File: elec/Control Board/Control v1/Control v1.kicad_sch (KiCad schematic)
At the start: 69 parts, among them J1 DB9_Female_MountingHoles, J10 Conn_02x12_Odd_Even, J11 Screw_Terminal_01x02, J14 Conn_01x10, J2 Conn_01x08, J25 Screw_Terminal_01x02, J3 Conn_01x08, J4 Conn_01x08, J5 Conn_01x08, J6 Conn_01x08, J7 Conn_01x10, J8 Conn_02x18_Odd_Even, J9 Conn_01x10

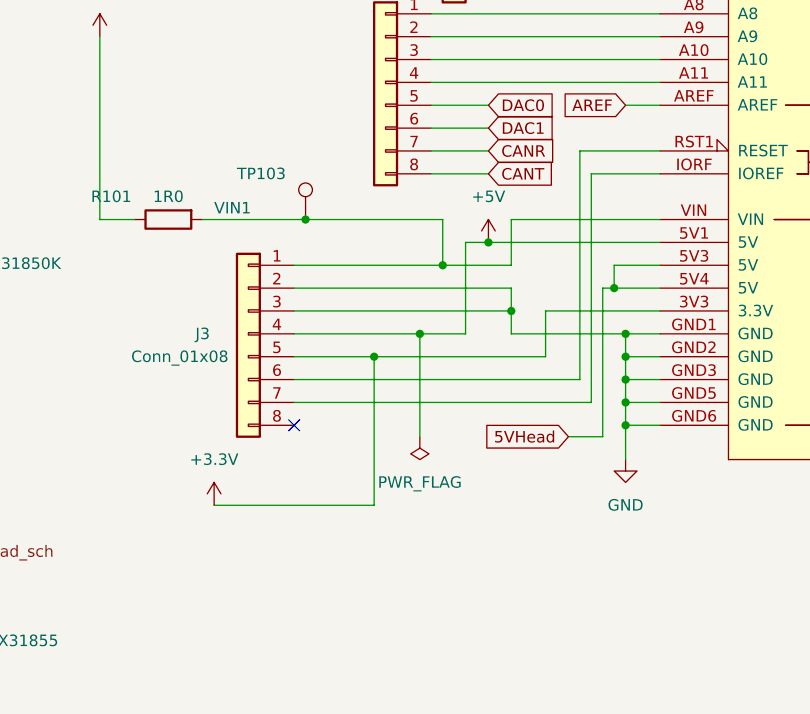
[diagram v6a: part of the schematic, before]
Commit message: Fixing some DRC errors on PCB.
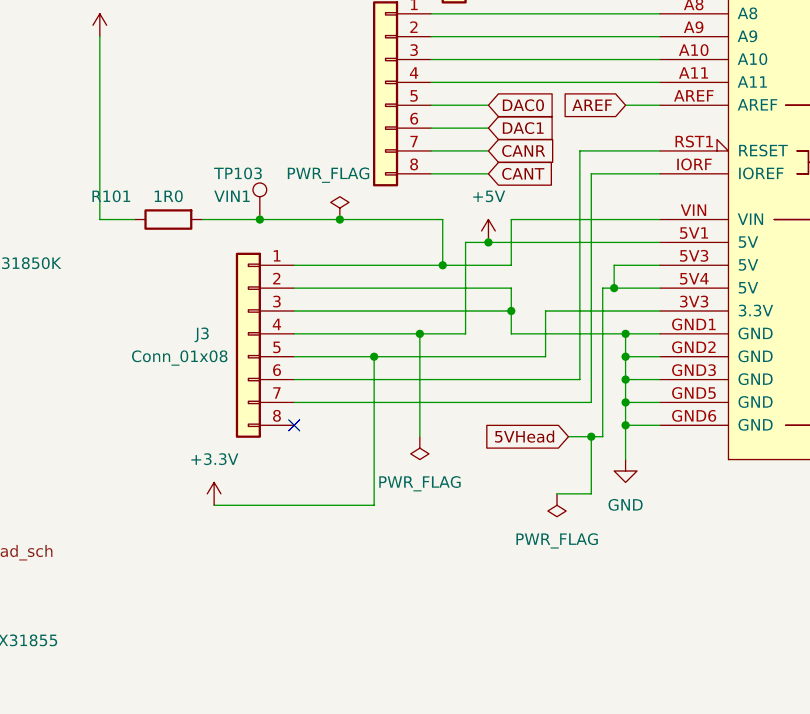
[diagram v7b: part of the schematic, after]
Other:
- moved on the sheet: TP103
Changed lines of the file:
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@@
     (comment 1 "Contributor: Lawrence Kinceloe")
   )
+  (junction (at 170.18 172.72) (diameter 0) (color 0 0 0 0)
+  )
   (junction (at 350.52 86.36) (diameter 0) (color 0 0 0 0)
   )
@@
   (junction (at 207.01 209.55) (diameter 0) (color 0 0 0 0)
   )
+  (junction (at 133.35 148.59) (diameter 0) (color 0 0 0 0)
+  )
   (junction (at 173.99 166.37) (diameter 0) (color 0 0 0 0)
   )
@@
   (junction (at 63.5 63.5) (diameter 0) (color 0 0 0 0)
   )
+  (junction (at 142.24 148.59) (diameter 0) (color 0 0 0 0)
+  )
   (junction (at 350.52 83.82) (diameter 0) (color 0 0 0 0)
   )
@@
   (junction (at 207.01 217.17) (diameter 0) (color 0 0 0 0)
   )
-  (junction (at 138.43 148.59) (diameter 0) (color 0 0 0 0)
-  )
   (junction (at 135.89 62.23) (diameter 0) (color 0 0 0 0)
   )
@@
     (stroke (width 0) (type default))
   )
+  (wire (pts (xy 142.24 148.59) (xy 153.67 148.59))
+    (stroke (width 0) (type default))
+  )
   (wire (pts (xy 243.84 125.73) (xy 246.38 125.73))
     (stroke (width 0) (type default))
@@
     (stroke (width 0) (type default))
   )
+  (wire (pts (xy 166.37 179.07) (xy 170.18 179.07))
+    (stroke (width 0) (type default))
+  )
   (wire (pts (xy 133.35 223.52) (xy 125.73 223.52))
     (stroke (width 0) (type default))
@@
     (stroke (width 0) (type default))
   )
-  (wire (pts (xy 167.64 172.72) (xy 171.45 172.72))
+  (wire (pts (xy 167.64 172.72) (xy 170.18 172.72))
+    (stroke (width 0) (type default))
+  )
+  (wire (pts (xy 170.18 179.07) (xy 170.18 172.72))
     (stroke (width 0) (type default))
   )
@@
     (stroke (width 0) (type default))
   )
-  (wire (pts (xy 127 148.59) (xy 138.43 148.59))
+  (wire (pts (xy 127 148.59) (xy 133.35 148.59))
     (stroke (width 0) (type default))
   )
@@
     (stroke (width 0) (type default))
   )
-  (wire (pts (xy 138.43 148.59) (xy 153.67 148.59))
+  (wire (pts (xy 133.35 148.59) (xy 142.24 148.59))
     (stroke (width 0) (type default))
   )
@@
     (stroke (width 0) (type default))
   )
+  (wire (pts (xy 170.18 172.72) (xy 171.45 172.72))
+    (stroke (width 0) (type default))
+  )
   (wire (pts (xy 381 45.72) (xy 381 66.04))
     (stroke (width 0) (type default))
@@
     )
   )
+  (symbol (lib_id "power:PWR_FLAG") (at 142.24 148.59 0) (unit 1)
+    (in_bom yes) (on_board yes) (dnp no)
+    (property "Reference" "#FLG07" (at 142.24 146.685 0)
+      (effects (font (size 1.27 1.27)) hide)
+    )
+    (property "Value" "PWR_FLAG" (at 140.97 143.51 0)
+      (effects (font (size 1.27 1.27)))
+    )
+    (property "Footprint" "" (at 142.24 148.59 0)
+      (effects (font (size 1.27 1.27)) hide)
+    )
+    (property "Datasheet" "~" (at 142.24 148.59 0)
+      (effects (font (size 1.27 1.27)) hide)
+    )
+    (pin "1")
+    (instances
+      (project "Control v1"
+        (path "/c68c9deb-8d4d-42f0-adf8-4d3022f4ee59"
+          (reference "#FLG07") (unit 1)
+        )
+      )
+    )
+  )
   (symbol (lib_id "power:GND") (at 173.99 175.26 0) (unit 1)
     (in_bom yes) (on_board yes) (dnp no) (fields_autoplaced)
@@
     )
   )
-  (symbol (lib_id "Connector:TestPoint") (at 138.43 148.59 0) (unit 1)
+  (symbol (lib_id "Connector:TestPoint") (at 133.35 148.59 0) (unit 1)
     (in_bom yes) (on_board yes) (dnp no)
-    (property "Reference" "TP103" (at 130.81 143.51 0)
+    (property "Reference" "TP103" (at 128.27 143.51 0)
       (effects (font (size 1.27 1.27)) (justify left))
     )
-    (property "Value" "VIN1" (at 128.27 147.32 0)
+    (property "Value" "VIN1" (at 128.27 146.05 0)
       (effects (font (size 1.27 1.27)) (justify left))
     )
-    (property "Footprint" "TestPoint:TestPoint_Loop_D2.54mm_Drill1.5mm_Beaded" (at 143.51 148.59 0)
+    (property "Footprint" "TestPoint:TestPoint_Loop_D2.54mm_Drill1.5mm_Beaded" (at 138.43 148.59 0)
       (effects (font (size 1.27 1.27)) hide)
     )
-    (property "Datasheet" "~" (at 143.51 148.59 0)
+    (property "Datasheet" "~" (at 138.43 148.59 0)
       (effects (font (size 1.27 1.27)) hide)
     )
-    (property "AssemblyType" "HAND" (at 138.43 148.59 0)
+    (property "AssemblyType" "HAND" (at 133.35 148.59 0)
       (effects (font (size 1.27 1.27)) hide)
     )
@@
         )
       )
+    )
+  )
+  (symbol (lib_id "power:PWR_FLAG") (at 166.37 179.07 180) (unit 1)
+    (in_bom yes) (on_board yes) (dnp no) (fields_autoplaced)
+    (property "Reference" "#FLG02" (at 166.37 180.975 0)
+      (effects (font (size 1.27 1.27)) hide)
+    )
+    (property "Value" "PWR_FLAG" (at 166.37 184.15 0)
+      (effects (font (size 1.27 1.27)))
+    )
+    (property "Footprint" "" (at 166.37 179.07 0)
+      (effects (font (size 1.27 1.27)) hide)
+    )
+    (property "Datasheet" "~" (at 166.37 179.07 0)
+      (effects (font (size 1.27 1.27)) hide)
+    )
+    (pin "1")
+    (instances
+      (project "Control v1"
+        (path "/c68c9deb-8d4d-42f0-adf8-4d3022f4ee59"
+          (reference "#FLG02") (unit 1)
+        )
+      )

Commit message: Update parts in schematic for BOM generation.
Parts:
- J1: AssemblyType (none) -> HAND; Cost (none) -> 0.2718; Distributor 1 (none) -> JLCPCB; Distributor 1 PN (none) -> C141882; MPN (none) -> D-DMR009PF-D002; Manufacturer (none) -> Ckmtw(Shenzhen Cankemeng)
- J10: Cost (none) -> 1000000; Distributor 2 JLCPCB -> JLCPCB ?https://jlcpcb.com/partdetail/566831-B24B_XADSS_N_A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; Distributor 2 PN https://jlcpcb.com/partdetail/Cnjm-CNJMA2006WV_2X12P9T/C283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 -> ? https://jlcpcb.com/partdetail/Cnjm-CNJMA2006WV_2X12P9T/C2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
- J11, J25: Distributor 1 PN C2915639 -> C918120; MPN (none) -> DB125-2.54-2P-GN-S; Manufacturer (none) -> DIBO
- J8: AssemblyType (none) -> HAND; Cost (none) -> 0.3441; Distributor 1 (none) -> JLCPCB; Distributor 1 PN (none) -> C132131
- R101: Cost 0.0015 -> 0.0012; Distributor 1 PN (none) -> C23163; MPN RMC060315%N -> 0603WAF4704T5E
- TP103: Cost (none) -> NA
- TP103: Cost (none) -> 0
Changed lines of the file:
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@@
       (effects (font (size 1.27 1.27)) hide)
     )
-    (property "Datasheet" "~" (at 312.42 138.43 0)
+    (property "Datasheet" "C132131_DS1023-2_18SF11.pdf" (at 312.42 138.43 0)
+      (effects (font (size 1.27 1.27)) hide)
+    )
+    (property "AssemblyType" "HAND" (at 312.42 138.43 0)
+      (effects (font (size 1.27 1.27)) hide)
+    )
+    (property "Cost" "0.3441" (at 312.42 138.43 0)
+      (effects (font (size 1.27 1.27)) hide)
+    )
+    (property "Description" "2.54mm 2.54mm 双排 36P Straight 2x18P Plugin,P=2.54mm Female Headers ROHS" (at 312.42 138.43 0)
+      (effects (font (size 1.27 1.27)) hide)
+    )
+    (property "Distributor 1" "JLCPCB" (at 312.42 138.43 0)
+      (effects (font (size 1.27 1.27)) hide)
+    )
+    (property "Distributor 1 PN" "C132131" (at 312.42 138.43 0)
       (effects (font (size 1.27 1.27)) hide)
     )
@@
       (effects (font (size 1.27 1.27)) hide)
     )
+    (property "Cost" "NA" (at 193.04 39.37 0)
+      (effects (font (size 1.27 1.27)) hide)
+    )
     (pin "1")
     (instances
@@
       (effects (font (size 1.27 1.27)) hide)
     )
+    (property "Cost" "NA" (at 135.89 57.15 0)
+      (effects (font (size 1.27 1.27)) hide)
+    )
     (pin "1")
     (instances
@@
       (effects (font (size 1.27 1.27)) hide)
     )
+    (property "Cost" "NA" (at 48.26 41.91 0)
+      (effects (font (size 1.27 1.27)) hide)
+    )
     (pin "1")
     (instances
@@
       (effects (font (size 1.27 1.27)) hide)
     )
-    (property "Distributor 1 PN" "C2915639" (at 394.97 205.74 0)
+    (property "Distributor 1 PN" "C918120" (at 394.97 205.74 0)
+      (effects (font (size 1.27 1.27)) hide)
+    )
+    (property "MPN" "DB125-2.54-2P-GN-S" (at 394.97 205.74 0)
+      (effects (font (size 1.27 1.27)) hide)
+    )
+    (property "Manufacturer" "DIBO" (at 394.97 205.74 0)
       (effects (font (size 1.27 1.27)) hide)
     )
@@
       (effects (font (size 1.27 1.27)) hide)
     )
+    (property "Cost" "NA" (at 129.54 48.26 0)
+      (effects (font (size 1.27 1.27)) hide)
+    )
     (pin "1")
     (instances
@@
       (effects (font (size 1.27 1.27)) hide)
     )
+    (property "Cost" "NA" (at 133.35 148.59 0)
+      (effects (font (size 1.27 1.27)) hide)
+    )
     (pin "1")
     (instances
@@
       (effects (font (size 1.27 1.27)) hide)
     )
-    (property "Datasheet" "~" (at 190.5 218.44 0)
+    (property "Datasheet" "C23163_0603WAF4704T5E.pdf" (at 190.5 218.44 0)
       (effects (font (size 1.27 1.27)) hide)
     )
@@
       (effects (font (size 1.27 1.27)) hide)
     )
-    (property "Distributor 1 PN" "" (at 190.5 218.44 90)
+    (property "Distributor 1 PN" "C23163" (at 190.5 218.44 90)
       (effects (font (size 1.27 1.27)) hide)
     )
@@
       (effects (font (size 1.27 1.27)) hide)
     )
-    (property "MPN" "RMC060315%N" (at 190.5 218.44 90)
+    (property "MPN" "0603WAF4704T5E" (at 190.5 218.44 90)
       (effects (font (size 1.27 1.27)) hide)
     )
-    (property "Description" "0.1W ±5% 1Ω 0603 Chip Resistor - Surface Mount ROHS" (at 190.5 218.44 0)
+    (property "Description" "100mW Thick Film Resistors ±100ppm/℃ ±1% 4.7MΩ 0603 Chip Resistor - Surface Mount ROHS" (at 190.5 218.44 0)
       (effects (font (size 1.27 1.27)) hide)
     )
@@
       (effects (font (size 1.27 1.27)) hide)
     )
-    (property "Cost" "0.0015" (at 190.5 218.44 0)
+    (property "Cost" "0.0012" (at 190.5 218.44 0)
       (effects (font (size 1.27 1.27)) hide)
     )
@@
       (effects (font (size 1.27 1.27)) hide)
     )
+    (property "Cost" "0" (at 154.94 59.69 0)
+      (effects (font (size 1.27 1.27)) hide)
+    )
     (pin "1")
     (instances
@@
       (effects (font (size 1.27 1.27)) hide)
     )
-    (property "Distributor 1 PN" "C2915639" (at 394.97 173.99 0)
+    (property "Distributor 1 PN" "C918120" (at 394.97 173.99 0)
+      (effects (font (size 1.27 1.27)) hide)
+    )
+    (property "MPN" "DB125-2.54-2P-GN-S" (at 394.97 173.99 0)
+      (effects (font (size 1.27 1.27)) hide)
+    )
+    (property "Manufacturer" "DIBO" (at 394.97 173.99 0)
       (effects (font (size 1.27 1.27)) hide)
     )
@@
       (effects (font (size 1.27 1.27)) hide)
     )
-    (property "Distributor 2" "JLCPCB" (at 368.3 78.74 0)
+    (property "Distributor 2" "JLCPCB ?https://jlcpcb.com/partdetail/566831-B24B_XADSS_N_A_LF_SN/C545730?" (at 368.3 78.74 0)
+      (effects (font (size 1.27 1.27)) hide)
+    )
+    (property "Distributor 2 PN" "?  https://jlcpcb.com/partdetail/Cnjm-CNJMA2006WV_2X12P9T/C2834570 ?" (at 368.3 78.74 0)
       (effects (font (size 1.27 1.27)) hide)
     )
-    (property "Distributor 2 PN" "https://jlcpcb.com/partdetail/Cnjm-CNJMA2006WV_2X12P9T/C2834570" (at 368.3 78.74 0)
+    (property "Cost" "1000000" (at 368.3 78.74 0)
       (effects (font (size 1.27 1.27)) hide)
     )
@@
       (effects (font (size 1.27 1.27)) hide)
     )
+    (property "Cost" "0" (at 162.56 59.69 0)
+      (effects (font (size 1.27 1.27)) hide)
+    )
     (pin "1")
     (instances
@@
       (effects (font (size 1.27 1.27)) hide)
     )
-    (property "Distributor 1 PN" "C2915639" (at 394.97 234.95 0)
+    (property "Distributor 1 PN" "C918120" (at 394.97 234.95 0)
+      (effects (font (size 1.27 1.27)) hide)
+    )
+    (property "MPN" "DB125-2.54-2P-GN-S" (at 394.97 234.95 0)
+      (effects (font (size 1.27 1.27)) hide)
+    )
+    (property "Manufacturer" "DIBO" (at 394.97 234.95 0)
       (effects (font (size 1.27 1.27)) hide)
     )
@@
       (effects (font (size 1.27 1.27)) hide)
     )
-    (property "Datasheet" " ~" (at 46.99 71.12 0)
+    (property "Datasheet" "C141882_D-DMR009PF-D002.pdf" (at 46.99 71.12 0)
+      (effects (font (size 1.27 1.27)) hide)
+    )
+    (property "AssemblyType" "HAND" (at 46.99 71.12 0)
+      (effects (font (size 1.27 1.27)) hide)
+    )
+    (property "Cost" "0.2718" (at 46.99 71.12 0)
+      (effects (font (size 1.27 1.27)) hide)
+    )
+    (property "Description" "9P Female D-Sub Shrouded 2 3A -50℃~+105℃ Plugin D-Sub/DVI/HDMI Connectors ROHS" (at 46.99 71.12 0)
+      (effects (font (size 1.27 1.27)) hide)
+    )
+    (property "Distributor 1" "JLCPCB" (at 46.99 71.12 0)
+      (effects (font (size 1.27 1.27)) hide)
+    )
+    (property "Distributor 1 PN" "C141882" (at 46.99 71.12 0)
+      (effects (font (size 1.27 1.27)) hide)
+    )
+    (property "MPN" "D-DMR009PF-D002" (at 46.99 71.12 0)
+      (effects (font (size 1.27 1.27)) hide)
+    )
+    (property "Manufacturer" "Ckmtw(Shenzhen Cankemeng)" (at 46.99 71.12 0)
       (effects (font (size 1.27 1.27)) hide)
     )
@@
       (effects (font (size 1.27 1.27)) hide)
     )
-    (property "Distributor 1 PN" "C2915639" (at 400.05 46.99 0)
+    (property "Distributor 1 PN" "C918120" (at 400.05 46.99 0)
+      (effects (font (size 1.27 1.27)) hide)
+    )
+    (property "MPN" "DB125-2.54-2P-GN-S" (at 400.05 46.99 0)
+      (effects (font (size 1.27 1.27)) hide)
+    )
+    (property "Manufacturer" "DIBO" (at 400.05 46.99 0)
       (effects (font (size 1.27 1.27)) hide)
     )
@@
       (effects (font (size 1.27 1.27)) hide)
     )
+    (property "Cost" "NA" (at 394.97 186.69 0)
+      (effects (font (size 1.27 1.27)) hide)
+    )
     (pin "1")
     (instances
@@
       (effects (font (size 1.27 1.27)) hide)
     )
+    (property "Cost" "0" (at 204.47 41.91 0)
+      (effects (font (size 1.27 1.27)) hide)
+    )
     (pin "1")
     (instances
@@
       (effects (font (size 1.27 1.27)) hide)
     )
+    (property "Cost" "0" (at 182.88 41.91 0)
+      (effects (font (size 1.27 1.27)) hide)
+    )
     (pin "1")
     (instances
@@
       (effects (font (size 1.27 1.27)) hide)
     )
+    (property "Cost" "NA" (at 394.97 218.44 0)
+      (effects (font (size 1.27 1.27)) hide)
+    )
